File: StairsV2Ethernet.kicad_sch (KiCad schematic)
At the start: 0 parts

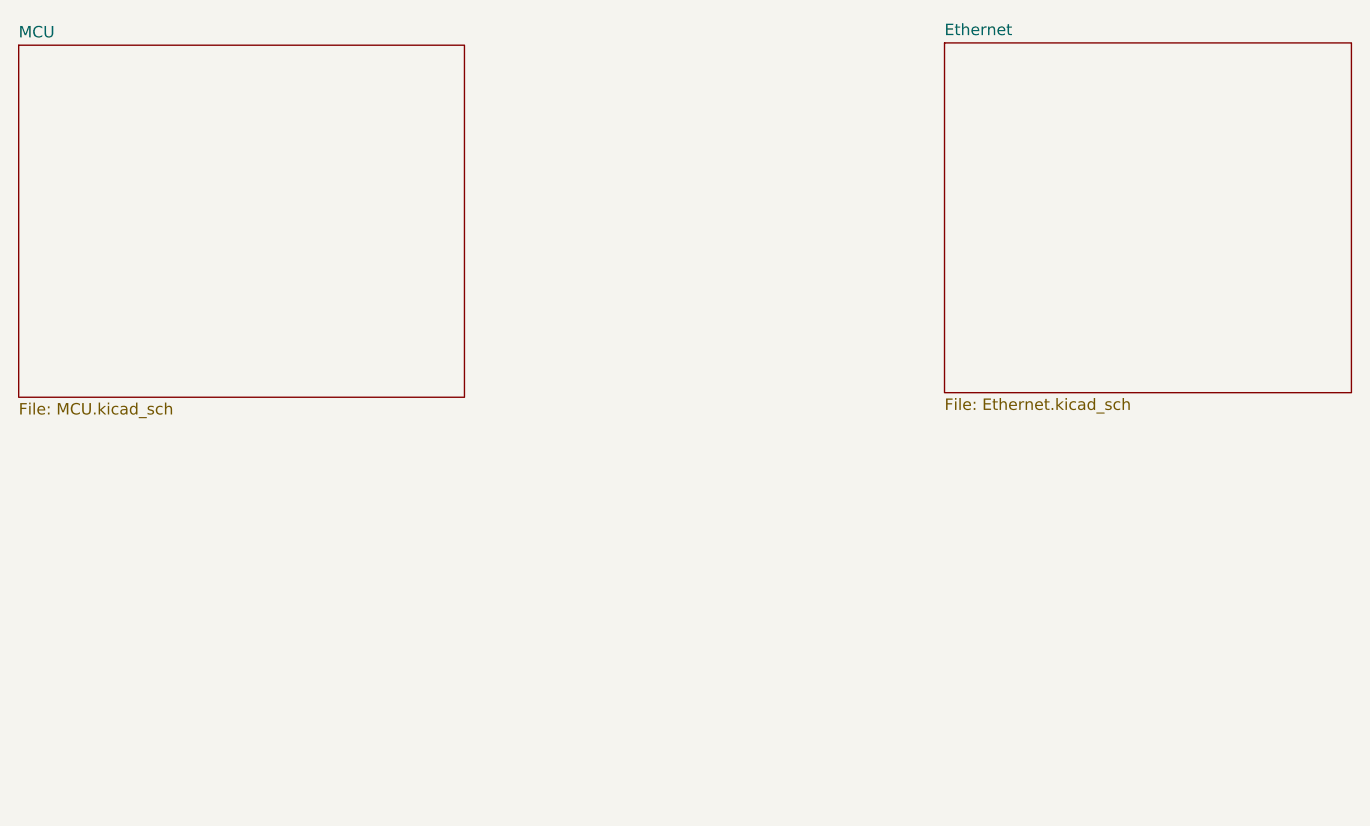
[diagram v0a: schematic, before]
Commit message: Ethernet W55000 controller added
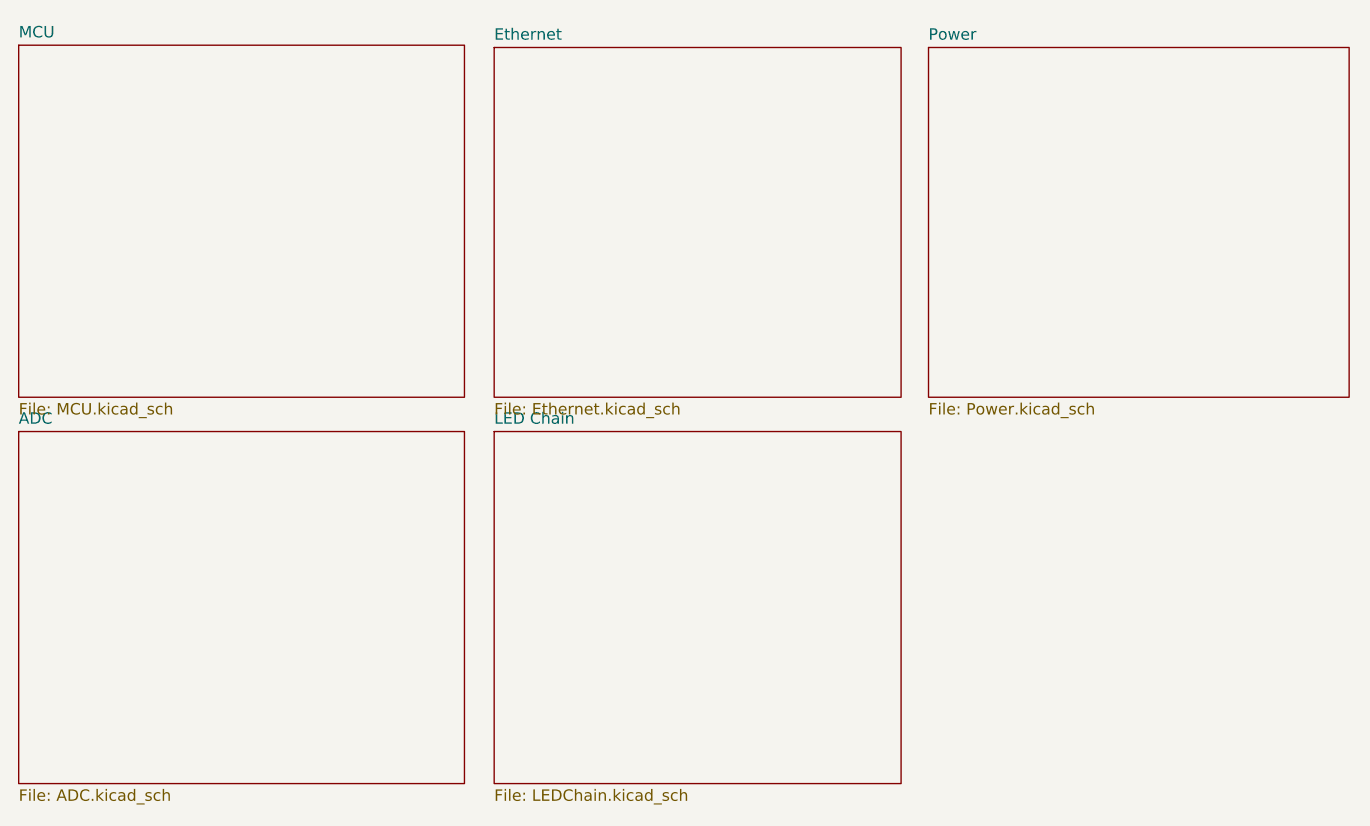
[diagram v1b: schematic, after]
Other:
- added sheet ADC (ADC.kicad_sch)
- added sheet LED Chain (LEDChain.kicad_sch)
- added sheet Power (Power.kicad_sch)
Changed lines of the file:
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@@
 	(paper "A4")
+	(sheet
+		(at 147.828 75.184)
+		(size 46.736 38.862)
+		(exclude_from_sim no)
+		(in_bom yes)
+		(on_board yes)
+		(dnp no)
+		(fields_autoplaced yes)
+		(stroke
+			(width 0.1524)
+			(type solid)
+		)
+		(fill
+			(color 0 0 0 0.0000)
+		)
+		(property "Sheetname" "Power"
+			(at 147.828 74.4724 0)
+			(effects
+				(font
+					(size 1.27 1.27)
+				)
+				(justify left bottom)
+			)
+		)
+		(property "Sheetfile" "Power.kicad_sch"
+			(at 147.828 114.6306 0)
+			(effects
+				(font
+					(size 1.27 1.27)
+				)
+				(justify left top)
+			)
+		)
+		(instances
+			(project "StairsV2Ethernet"
+				(path "/c74cf9f2-0af5-4a28-b0b6-05ce22add148"
+					(page "6")
+				)
+			)
+		)
+	)
 	(sheet
 		(at 46.736 74.93)
@@
 	)
 	(sheet
-		(at 149.606 74.676)
+		(at 99.568 117.856)
+		(size 45.212 39.116)
+		(exclude_from_sim no)
+		(in_bom yes)
+		(on_board yes)
+		(dnp no)
+		(fields_autoplaced yes)
+		(stroke
+			(width 0.1524)
+			(type solid)
+		)
+		(fill
+			(color 0 0 0 0.0000)
+		)
+		(property "Sheetname" "LED Chain"
+			(at 99.568 117.1444 0)
+			(effects
+				(font
+					(size 1.27 1.27)
+				)
+				(justify left bottom)
+			)
+		)
+		(property "Sheetfile" "LEDChain.kicad_sch"
+			(at 99.568 157.5566 0)
+			(effects
+				(font
+					(size 1.27 1.27)
+				)
+				(justify left top)
+			)
+		)
+		(instances
+			(project "StairsV2Ethernet"
+				(path "/c74cf9f2-0af5-4a28-b0b6-05ce22add148"
+					(page "5")
+				)
+			)
+		)
+	)
+	(sheet
+		(at 99.568 75.184)
 		(size 45.212 38.862)
 		(exclude_from_sim no)
@@
 		)
 		(property "Sheetname" "Ethernet"
-			(at 149.606 73.9644 0)
+			(at 99.568 74.4724 0)
 			(effects
 				(font
@@
 		)
 		(property "Sheetfile" "Ethernet.kicad_sch"
-			(at 149.606 114.1226 0)
+			(at 99.568 114.6306 0)
 			(effects
 				(font
@@
 				)
 			)
+		)
+	)
+	(sheet
+		(at 46.736 117.856)
+		(size 49.53 39.116)
+		(exclude_from_sim no)
+		(in_bom yes)
+		(on_board yes)
+		(dnp no)
+		(fields_autoplaced yes)
+		(stroke
+			(width 0.1524)
+			(type solid)
+		)
+		(fill
+			(color 0 0 0 0.0000)
+		)
+		(property "Sheetname" "ADC"
+			(at 46.736 117.1444 0)
+			(effects
+				(font
+					(size 1.27 1.27)
+				)
+				(justify left bottom)
+			)
+		)
+		(property "Sheetfile" "ADC.kicad_sch"
+			(at 46.736 157.5566 0)
+			(effects
+				(font
+					(size 1.27 1.27)
+				)
+				(justify left top)
+			)
+		)
+		(instances
+			(project "StairsV2Ethernet"
+				(path "/c74cf9f2-0af5-4a28-b0b6-05ce22add148"
+					(page "4")
+				)
+			)
